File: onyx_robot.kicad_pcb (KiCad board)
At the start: 2 copper layers, 50 x 50 mm, 32 parts, among them P1 EXT1, P2 EXT2, P3 READER, P4 FTDI, Q1 Q_NMOS_GDS, Q2 Q_NMOS_GDS, SW2 RESET, U1 ADP2301, U2 RELAY_SPDT, U3 ESP-12E

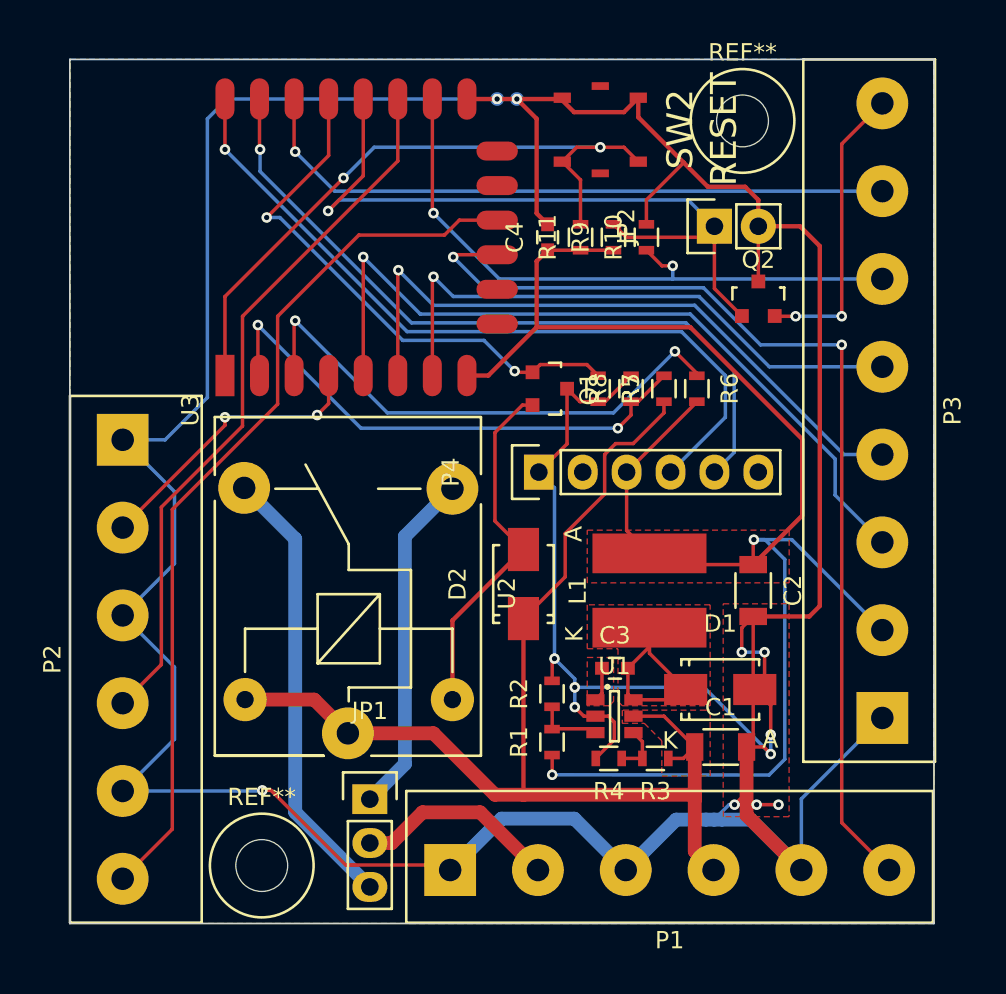
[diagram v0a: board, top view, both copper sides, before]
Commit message: Tidy-ups, increase track size
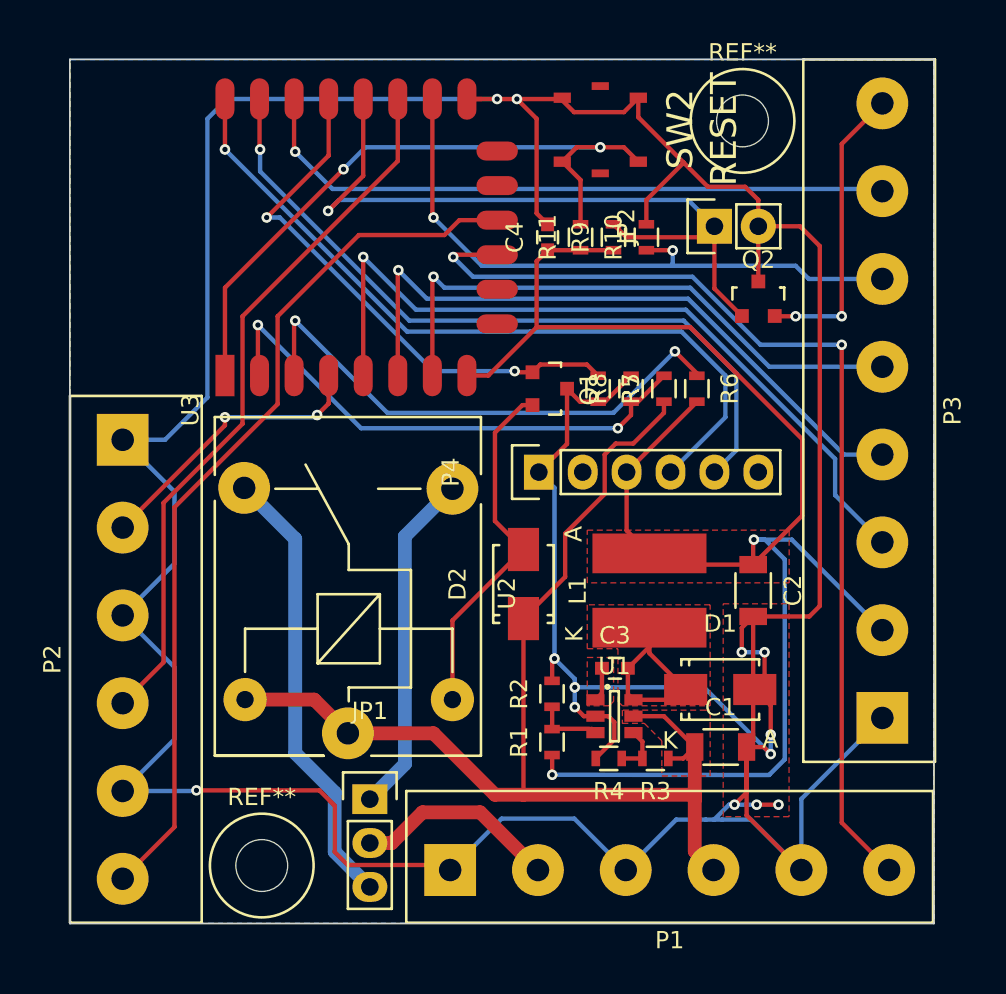
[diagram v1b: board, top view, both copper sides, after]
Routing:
- net GND: track 268.7 -> 270.3 mm
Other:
- net class Default: clearance 0.1524 -> 0.254; trace_width 0.2032 -> 0.254
- rule trace_clearance: 0.1524 -> 0.254
- rule trace_min: 0.1524 -> 0.254
- board text added: "timhawes.com/or1"

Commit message: Text tidied-up. Relay repositioned to give larger gaps. Mounting holes enlarged.
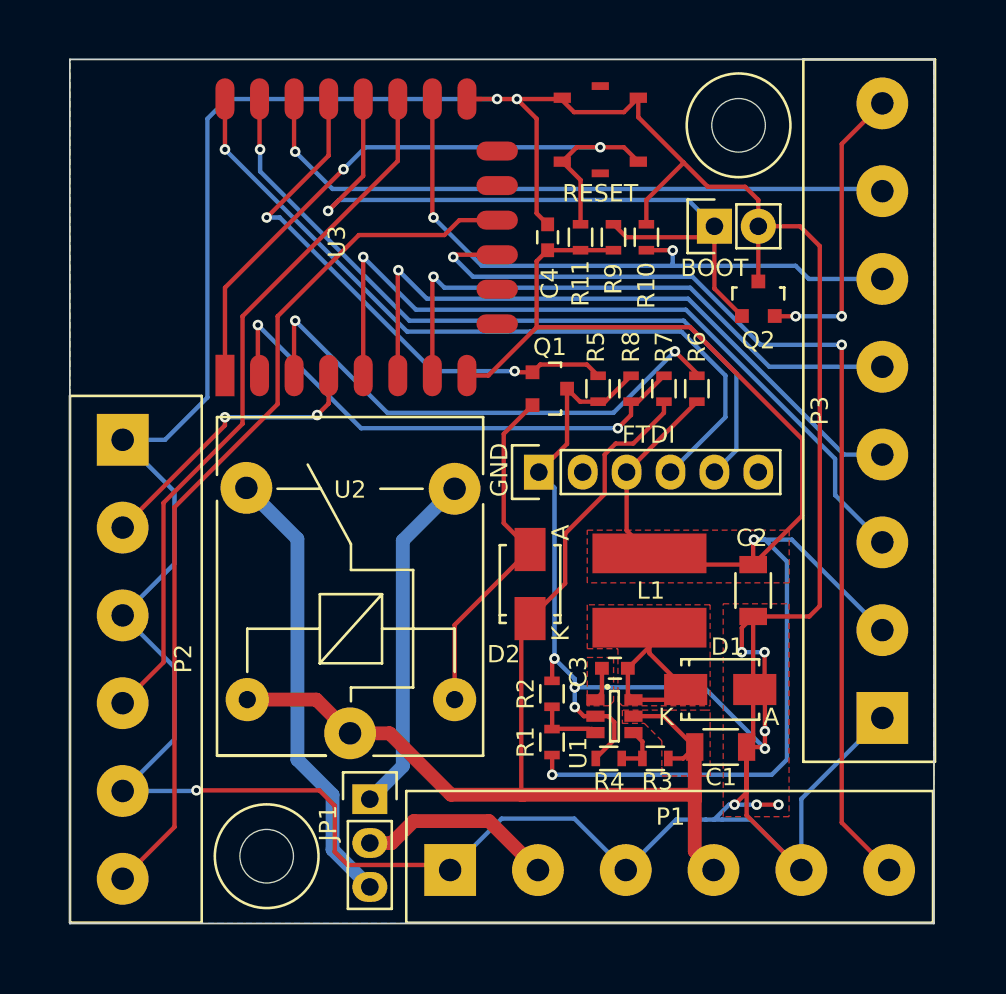
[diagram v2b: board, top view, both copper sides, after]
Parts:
- REF** (x2): footprint timhawes:MountingHole_M3 -> timhawes:MountingHole_M3+
- moved REF** 0.61 mm to (56.4, 86.1)
- moved D2 0.38 mm to (71.6, 70.4)
- moved REF** 0.34 mm to (83.7, 43.8)
- moved U2 0.13 mm to (61.2, 79.0)
- renumbered JP2 to BOOT, SW2 to RESET
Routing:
- net GND: track 270.3 -> 268.9 mm
- net Net-(D2-Pad2): track 20.7 -> 20.2 mm
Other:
- board text added: "12V"
- board text added: "12V_OUT"
- board text added: "3.3V"
- board text added: "CLK"
- board text added: "CS"
- board text added: "DOOR_SENSE"
- board text added: "EXIT"
- board text added: "GND"
- board text added: "LED"
- board text added: "MISO"
- board text added: "MOSI"
- board text added: "PIEZO"
- board text added: "SNIB"
- board text added: "TAMPER"
- board text added: "timhawes.com/or1 edinburghhacklab.com"
- board text removed: "timhawes.com/or1"

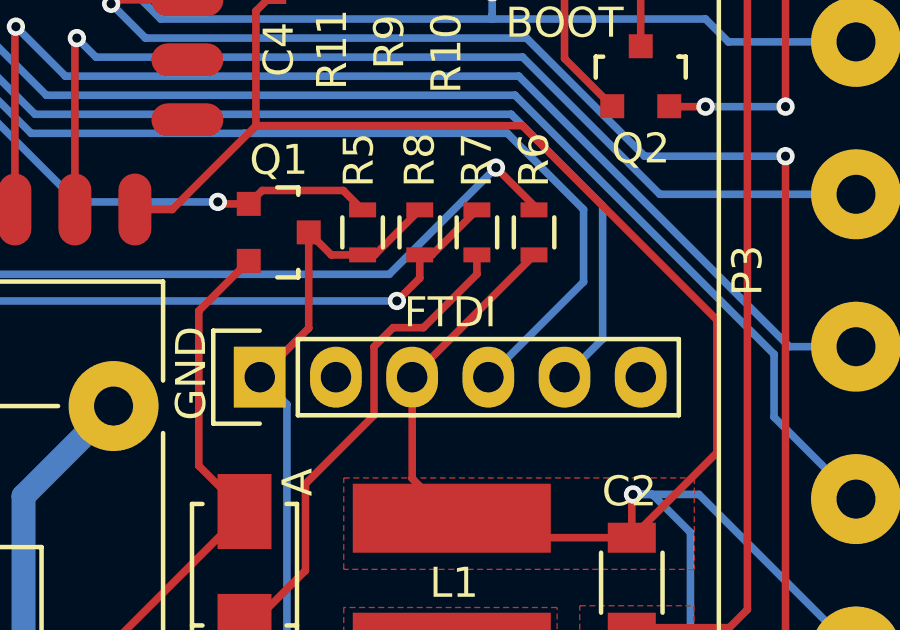
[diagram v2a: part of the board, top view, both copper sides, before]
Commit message: Restore FTDI reference text
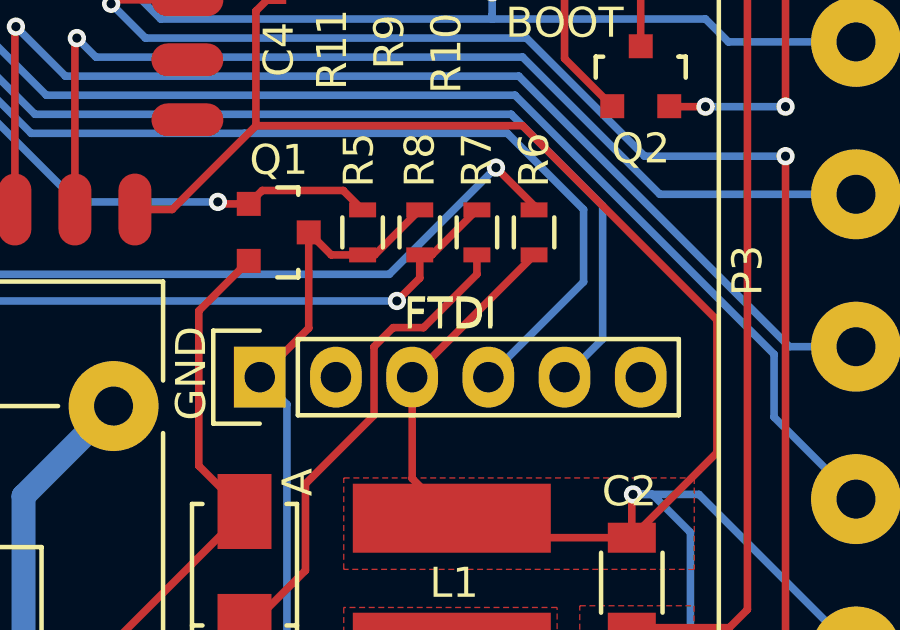
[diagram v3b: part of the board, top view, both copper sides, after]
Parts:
- renumbered P4 to FTDI
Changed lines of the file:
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@@
     (descr "Through hole pin header")
     (tags "pin header")
-    (fp_text reference P4 (at -2.231 6.342 180) (layer F.Fab)
+    (fp_text reference FTDI (at 2.087 6.342 180) (layer F.SilkS)
       (effects (font (size 1 1) (thickness 0.15)))
     )

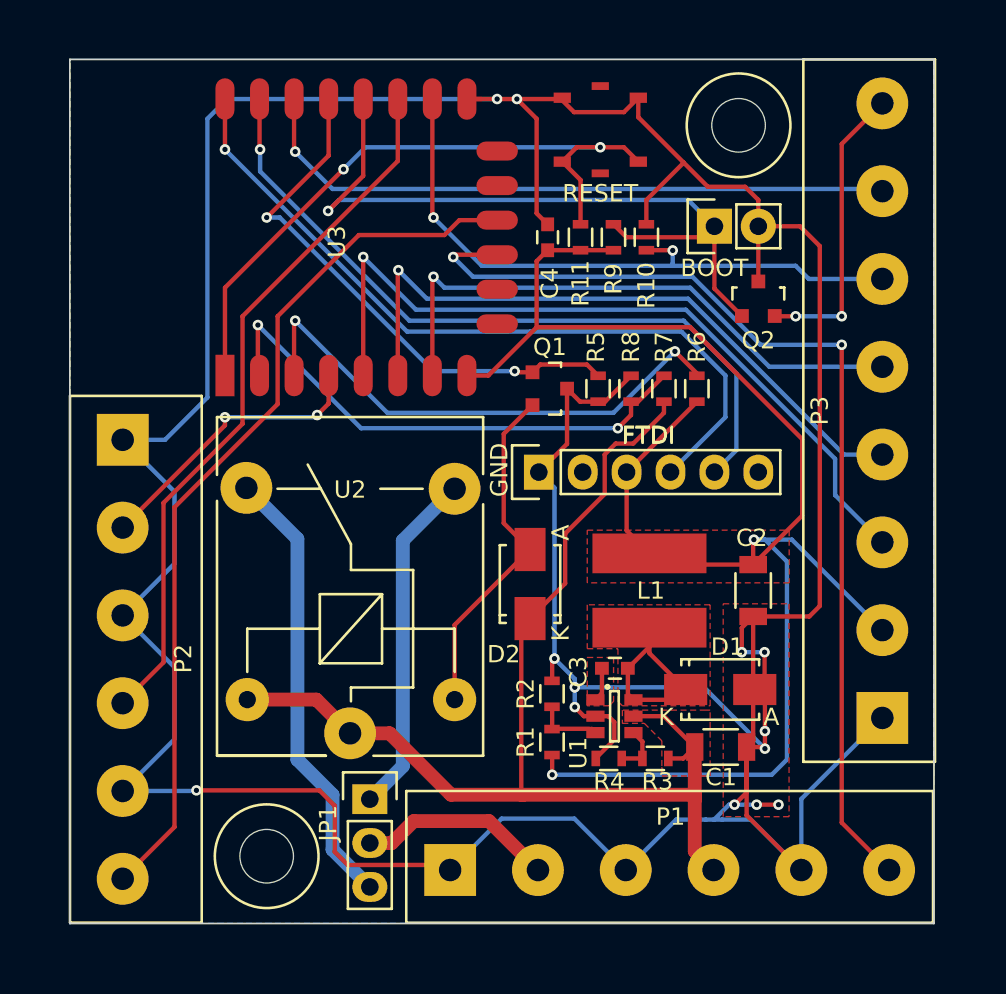
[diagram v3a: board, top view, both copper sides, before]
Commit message: Clean-up silkscreen labels
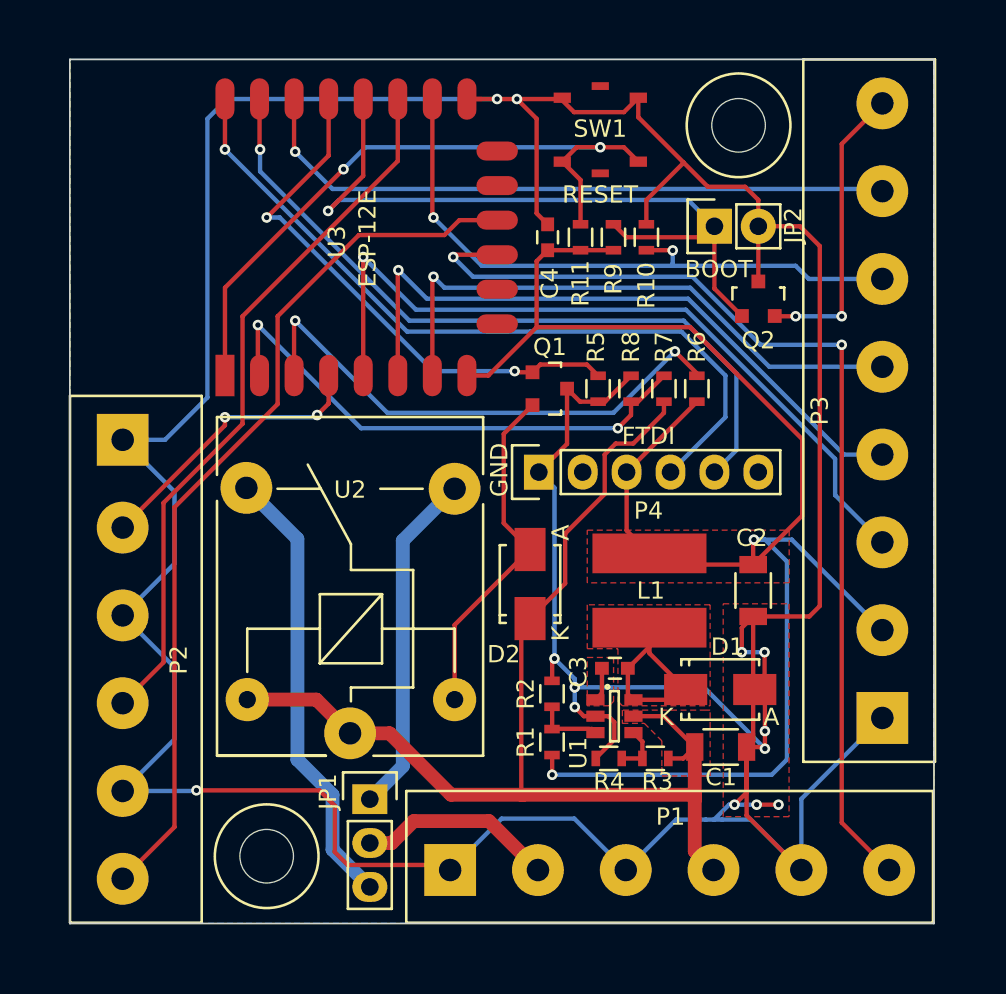
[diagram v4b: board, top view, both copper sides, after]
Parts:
- JP2: renamed from BOOT; value PROG -> BOOT
- renumbered FTDI to P4, RESET to SW1
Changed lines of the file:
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@@
     (aux_axis_origin 0 0)
     (grid_origin 44.95 39.95)
-    (visible_elements FFFEFFFF)
+    (visible_elements FFFFFFFF)
     (pcbplotparams
       (layerselection 0x010f0_80000001)
@@
       (psa4output false)
       (plotreference true)
-      (plotvalue false)
+      (plotvalue true)
       (plotinvisibletext false)
       (padsonsilk false)
@@
     (descr "Through hole pin header")
     (tags "pin header")
-    (fp_text reference BOOT (at -2.413 0 180) (layer F.SilkS)
-      (effects (font (size 1 1) (thickness 0.15)))
-    )
-    (fp_text value PROG (at 0 -3.1 90) (layer F.Fab)
+    (fp_text reference JP2 (at 0.055 4.564 90) (layer F.SilkS)
+      (effects (font (size 1 1) (thickness 0.15)))
+    )
+    (fp_text value BOOT (at -2.485 0.246 180) (layer F.SilkS)
       (effects (font (size 1 1) (thickness 0.15)))
     )
@@
   (module timhawes:Terminal_Block_5.08mm_x6 (layer F.Cu)
     (at 48.0568 74.71156 270)
-    (fp_text reference P2 (at -0.03556 -3.5052 270) (layer F.SilkS)
+    (fp_text reference P2 (at 0.03644 -3.2432 450) (layer F.SilkS)
       (effects (font (size 1 1) (thickness 0.15)))
     )
@@
     (descr "Through hole pin header")
     (tags "pin header")
-    (fp_text reference FTDI (at 2.087 6.342 180) (layer F.SilkS)
-      (effects (font (size 1 1) (thickness 0.15)))
-    )
-    (fp_text value FTDI (at 2.159 6.35 180) (layer F.SilkS)
+    (fp_text reference P4 (at -2.231 6.342 180) (layer F.SilkS)
+      (effects (font (size 1 1) (thickness 0.15)))
+    )
+    (fp_text value FTDI (at 2.087 6.342 180) (layer F.SilkS)
       (effects (font (size 1 1) (thickness 0.15)))
     )
@@
   (module timhawes:EVQPT5 (layer F.Cu)
     (at 75.692 44.069 90)
-    (fp_text reference RESET (at -3.683 0 180) (layer F.SilkS)
-      (effects (font (size 1 1) (thickness 0.15)))
-    )
-    (fp_text value RESET (at -0.127 0 180) (layer F.Fab)
-      (effects (font (size 1.5 1.5) (thickness 0.15)))
+    (fp_text reference SW1 (at 0.055 -0.008 180) (layer F.SilkS)
+      (effects (font (size 1 1) (thickness 0.15)))
+    )
+    (fp_text value RESET (at -3.755 -0.008 180) (layer F.SilkS)
+      (effects (font (size 1 1) (thickness 0.15)))
     )
     (pad 1 smd rect (at -1.85 -2.2 90) (size 0.6 1) (layers F.Cu F.Paste F.Mask)
@@
     (descr "Through hole pin header")
     (tags "pin header")
-    (fp_text reference JP1 (at -2.413 1.397 90) (layer F.SilkS)
+    (fp_text reference JP1 (at -2.421 -0.436 90) (layer F.SilkS)
       (effects (font (size 1 1) (thickness 0.15)))
     )
@@
       (effects (font (size 1 1) (thickness 0.15)))
     )
-    (fp_text value ESP-12E (at 8 1 90) (layer F.Fab)
-      (effects (font (size 1 1) (thickness 0.15)))
-    )
+    (fp_text value ESP-12E (at 7.929 8.247 90) (layer F.SilkS)
+      (effects (font (size 1 1) (thickness 0.15)))
+    )

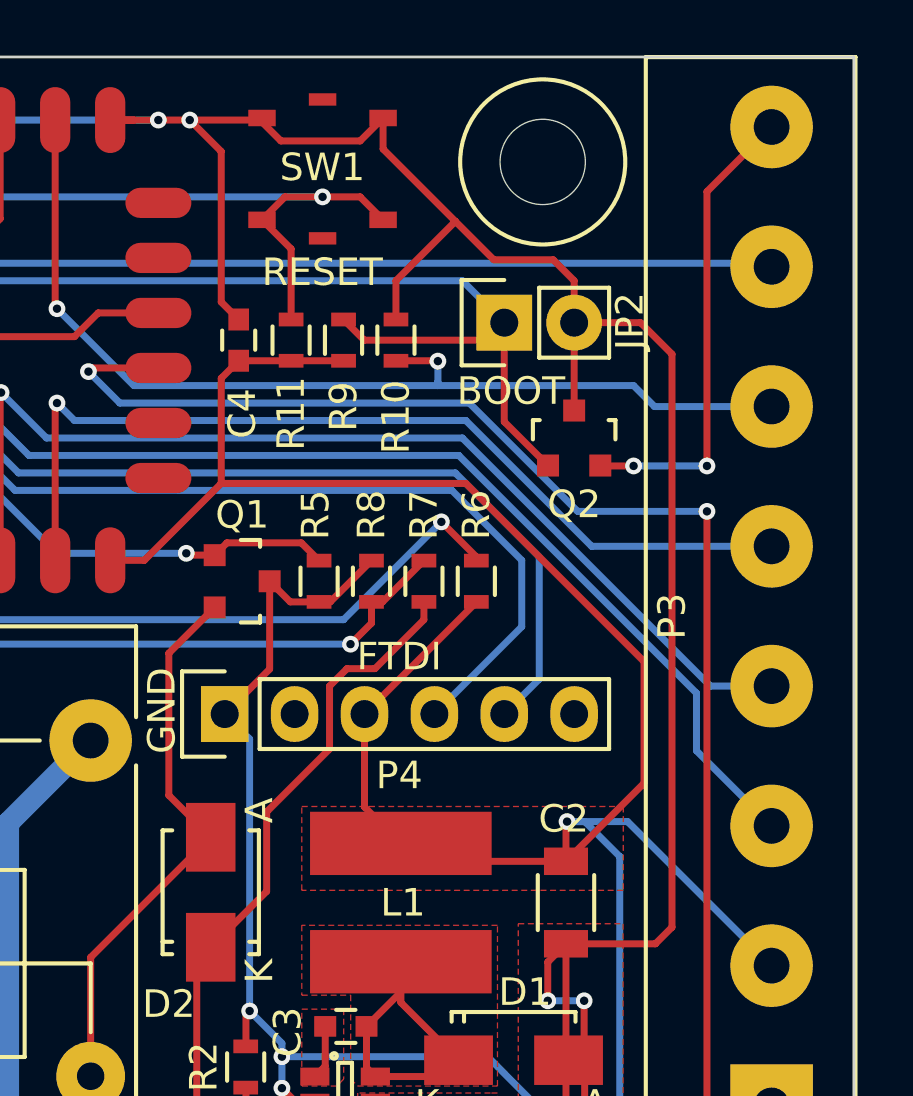
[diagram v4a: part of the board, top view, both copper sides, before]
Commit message: Change MOSFET SOT-23 pin ordering and adjust layout to match
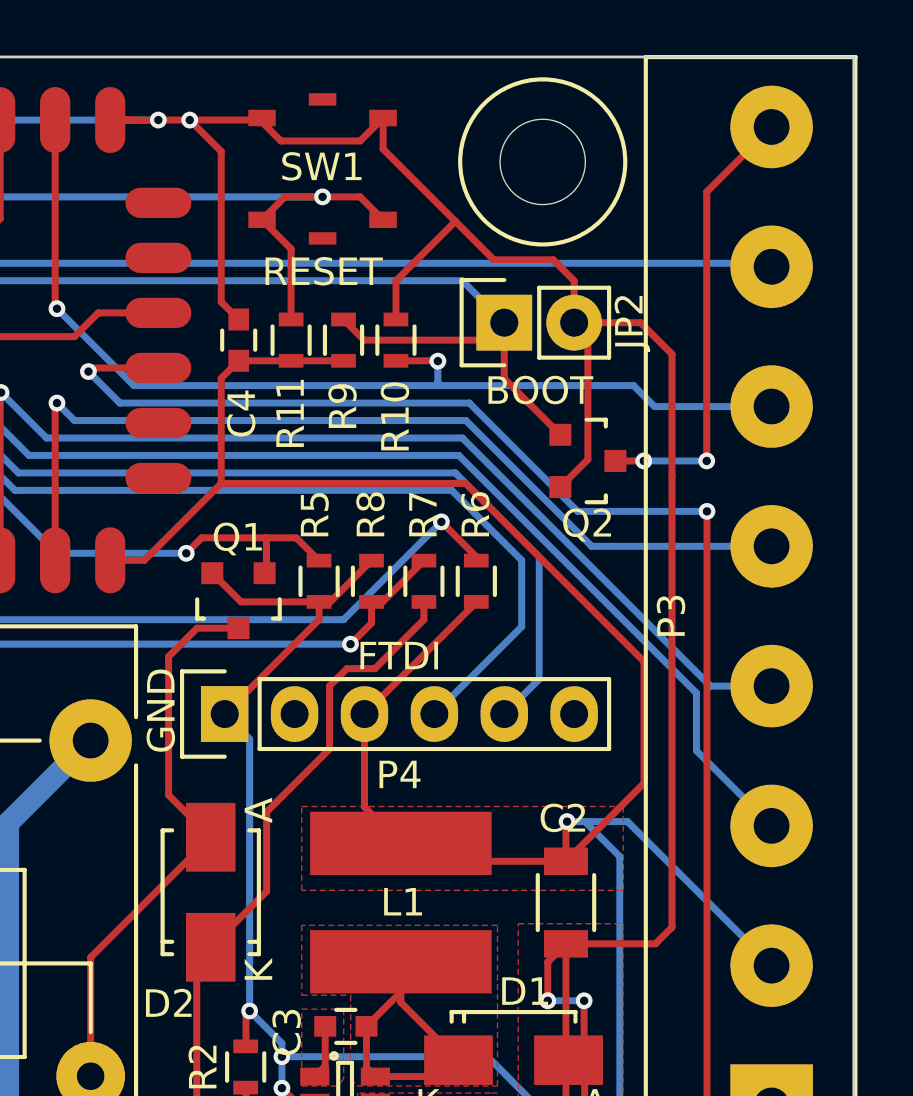
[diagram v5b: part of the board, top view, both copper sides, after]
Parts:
- Q1, Q2: value Q_NMOS_GDS -> Q_NMOS_GSD
- moved Q2 0.97 mm to (85.3, 54.7), turned to 270 degrees
- moved Q1 0.72 mm to (72.6, 59.8), turned to 180 degrees
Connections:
- Q1 pad 2: Net-(D2-Pad2) -> GND
- Q1 pad 3: GND -> Net-(D2-Pad2)
- Q2 pad 2: PIEZO -> GND
- Q2 pad 3: GND -> PIEZO
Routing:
- net GND: track 268.9 -> 274.5 mm
- net RELAY: track 31.7 -> 33.2 mm
- net GPIO0: track 42.8 -> 41.9 mm
- net PIEZO: track 17.2 -> 16.4 mm
